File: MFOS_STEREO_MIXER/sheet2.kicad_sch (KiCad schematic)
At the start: 54 parts, among them J10 Jack-DC, J11 Jack-DC, J12 Jack-DC, J13 Jack-DC, J15 Jack-DC, J16 Jack-DC, J18 Jack-DC, J19 Jack-DC, J5 Jack-DC, J6 Jack-DC, J8 Jack-DC, J9 Jack-DC, U6 TL072, U7 TL072

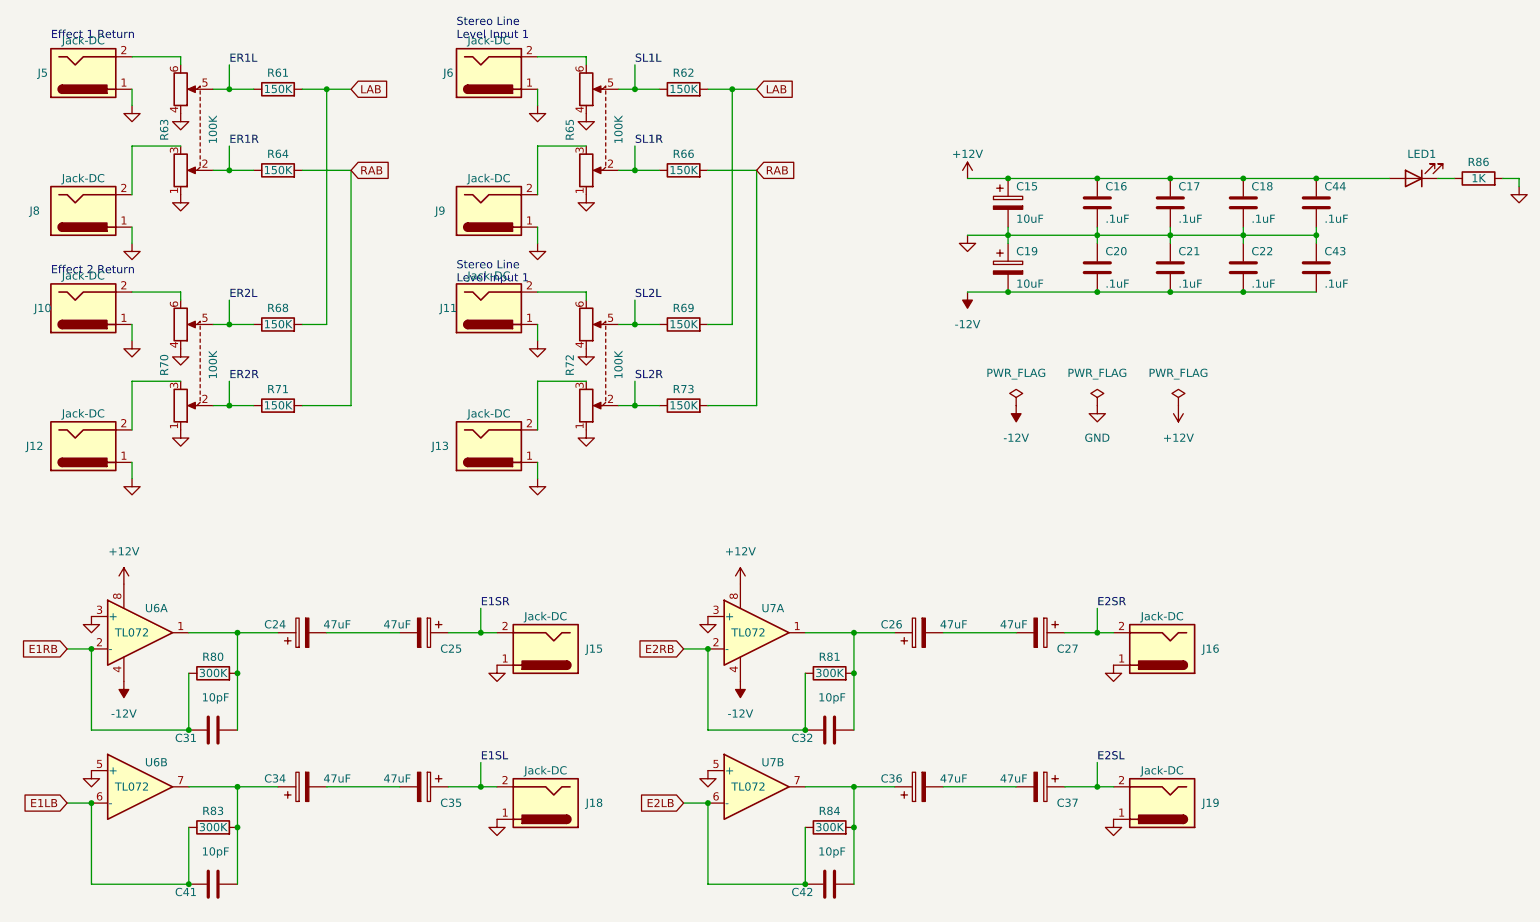
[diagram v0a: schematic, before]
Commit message: Split up design into different sheets
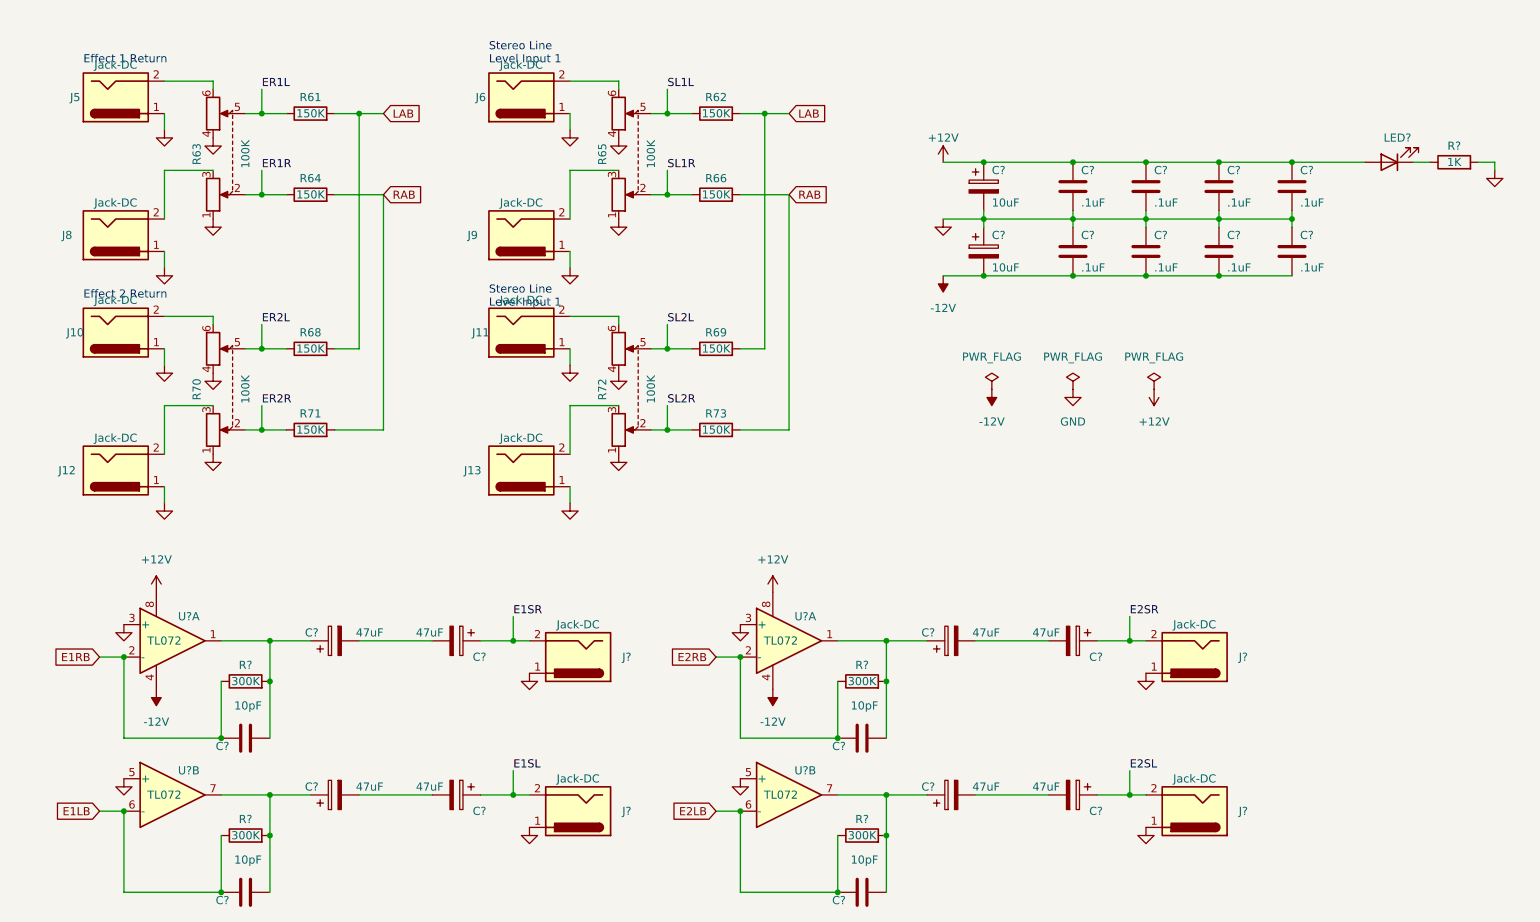
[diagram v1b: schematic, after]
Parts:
- removed C15, C19: 10uF, symbol Device:C_Polarized
- removed C16, C17, C18, C20, C21, C22, C43, C44: .1uF, symbol Device:C
- removed C24, C25, C26, C27, C34, C35, C36, C37: 47uF, symbol Device:C_Polarized
- removed C31, C32, C41, C42: 10pF, symbol Device:C
- removed J15, J16, J18, J19: Jack-DC, symbol Connector:Jack-DC
- removed LED1: LED, symbol Device:LED
- removed R80, R81, R83, R84: 300K, symbol Device:R
- removed R86: 1K, symbol Device:R
- removed U6, U7: TL072, symbol Amplifier_Operational:TL072
- added C? (x8): .1uF, symbol Device:C
- added C? (x8): 47uF, symbol Device:C_Polarized
- added C? (x4): 10pF, symbol Device:C
- added C? (x2): 10uF, symbol Device:C_Polarized
- added J? (x4): Jack-DC, symbol Connector:Jack-DC
- added LED?: LED, symbol Device:LED
- added R? (x4): 300K, symbol Device:R
- added R?: 1K, symbol Device:R
- added U? (x6): TL072, symbol Amplifier_Operational:TL072
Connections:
- net +12V: now also C?.1, C?.1, C?.1, C?.1, C?.1, LED?.2 (A), U?.8 (V+), U?.8 (V+)
- net -12V: now also C?.2, C?.2, C?.2, C?.2, C?.2, U?.4 (V-), U?.4 (V-)
- net E1LB: now also C?.1, R?.1, U?.6 (-)
- net E1RB: now also C?.1, R?.1, U?.2 (-)
- net E1SL: now also C?.1, J?.2
- net E1SR: now also C?.1, J?.2
- net E2LB: now also C?.1, R?.1, U?.6 (-)
- net E2RB: now also C?.1, R?.1, U?.2 (-)
- net E2SL: now also C?.1, J?.2
- net E2SR: now also C?.1, J?.2
- net GND: now also C?.1, C?.1, C?.1, C?.1, C?.1, C?.2, C?.2, C?.2, C?.2, C?.2, J?.1, J?.1, J?.1, J?.1, R?.2, U?.3 (+), U?.3 (+), U?.5 (+), U?.5 (+)
- new net: C?.1, C?.2, R?.2, U?.7 (x2)
- new net: C?.1, C?.2, R?.2, U?.1 (x2)
- new net: C?.2, C?.2 (x4)
- new net: LED?.1 (K), R?.1
